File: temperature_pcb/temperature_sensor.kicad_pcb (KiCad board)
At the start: 2 copper layers, 167.6 x 94 mm, 15 parts, among them J1 Screw_Terminal_01x02, M1 MAX31865-adafruit-module, M10 MAX31865-adafruit-module, M11 MAX31865-adafruit-module, M12 MAX31865-adafruit-module, M13 MAX31865-adafruit-module, M2 MAX31865-adafruit-module, M3 MAX31865-adafruit-module, M4 MAX31865-adafruit-module, M5 MAX31865-adafruit-module, M6 MAX31865-adafruit-module, M7 MAX31865-adafruit-module, M8 MAX31865-adafruit-module, M9 MAX31865-adafruit-module

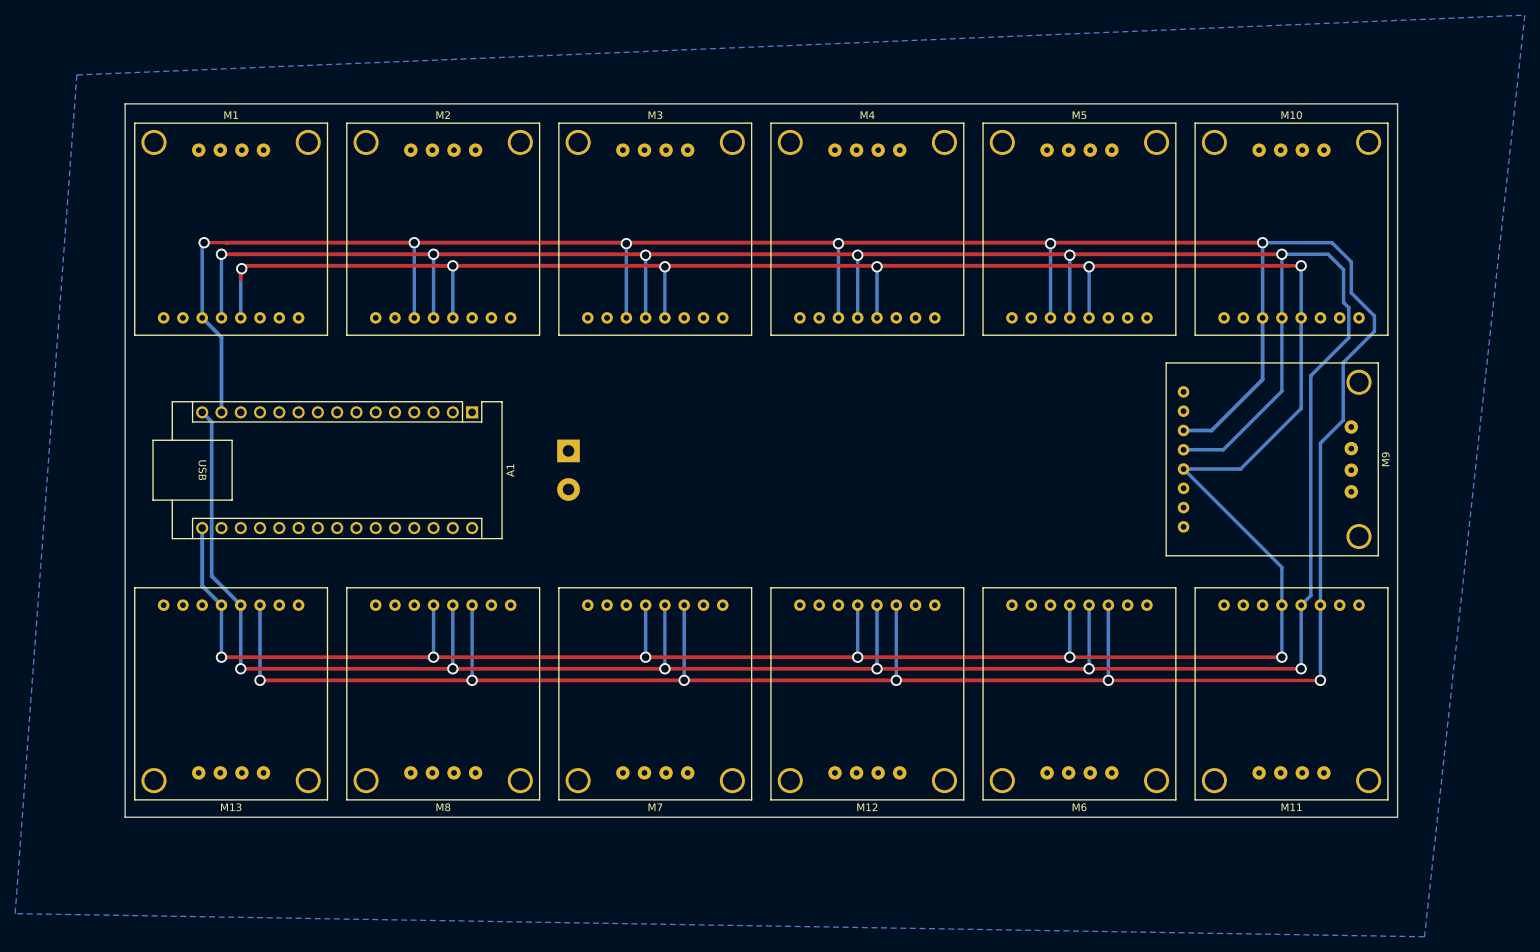
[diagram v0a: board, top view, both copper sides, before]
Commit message: first version of the pcb for the temperature sensors
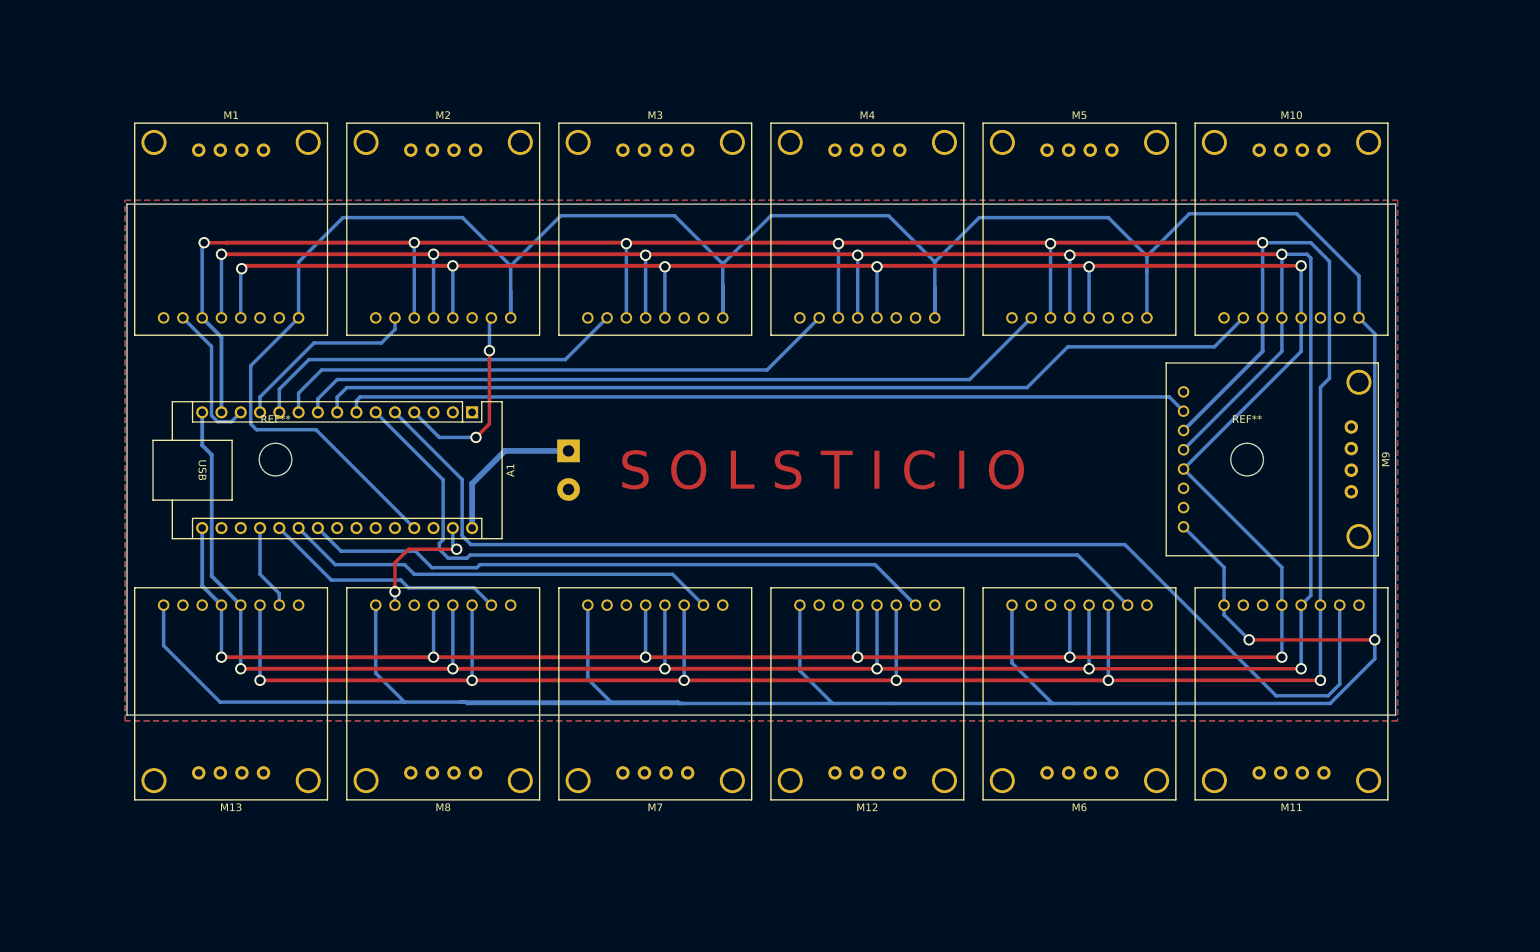
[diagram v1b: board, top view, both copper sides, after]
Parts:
- added REF**: MountingHole_4.3mm_M4, MountingHole:MountingHole_4.3mm_M4, F.Cu at (254.5, 105.3)
- added REF**: MountingHole_4.3mm_M4, MountingHole:MountingHole_4.3mm_M4, F.Cu at (126.5, 105.3)
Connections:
- A1 pad 27: unconnected-(A1-+5V-Pad27) -> +5V
- M1 pad 2: CS0 -> CS8
- M10 pad 2: CS8 -> CS3
- M11 pad 2: CS9 -> CS0
- M12 pad 2: CS10 -> CS12
- M13 pad 2: CS12 -> CS9
- M2 pad 2: CS1 -> CS7
- M3 pad 2: CS2 -> CS6
- M4 pad 2: CS3 -> CS5
- M6 pad 2: CS5 -> CS1
- M8 pad 2: CS6 -> CS10
- M9 pad 2: CS7 -> CS2
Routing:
- net +5V: track 0.00 -> 603.4 mm, vias 0 -> 2
- net CS0: track 0.00 -> 155.3 mm
- net CS3: track 0.00 -> 125.7 mm
- net CS1: track 0.00 -> 116.0 mm
- net CS2: track 0.00 -> 111.5 mm
- net CS4: track 0.00 -> 100.2 mm
- net CS12: track 0.00 -> 83.3 mm
- net CS5: track 0.00 -> 75.2 mm
- net CS11: track 0.00 -> 57.5 mm
- net CS6: track 0.00 -> 50.1 mm
- net GND: track 0.00 -> 43.5 mm, vias 0 -> 4
- net CS10: track 0.00 -> 32.1 mm
- net CS7: track 0.00 -> 25.0 mm
- net Net-(A1-VIN): track 0.00 -> 20.3 mm
- net CS8: track 0.00 -> 19.1 mm
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- added copper zone on F.Cu, net GND
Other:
- board size 167.6 x 94 mm -> 167.1 x 67.3 mm
- board text added: "S O L S T I C I O"
